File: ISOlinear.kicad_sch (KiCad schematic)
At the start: 23 parts, among them J1 USB_C_Receptacle_USB2.0, J2 Conn_01x20, J3 Conn_01x20, U1 STM32F072CBT6, U2 PRTR5V0U2X

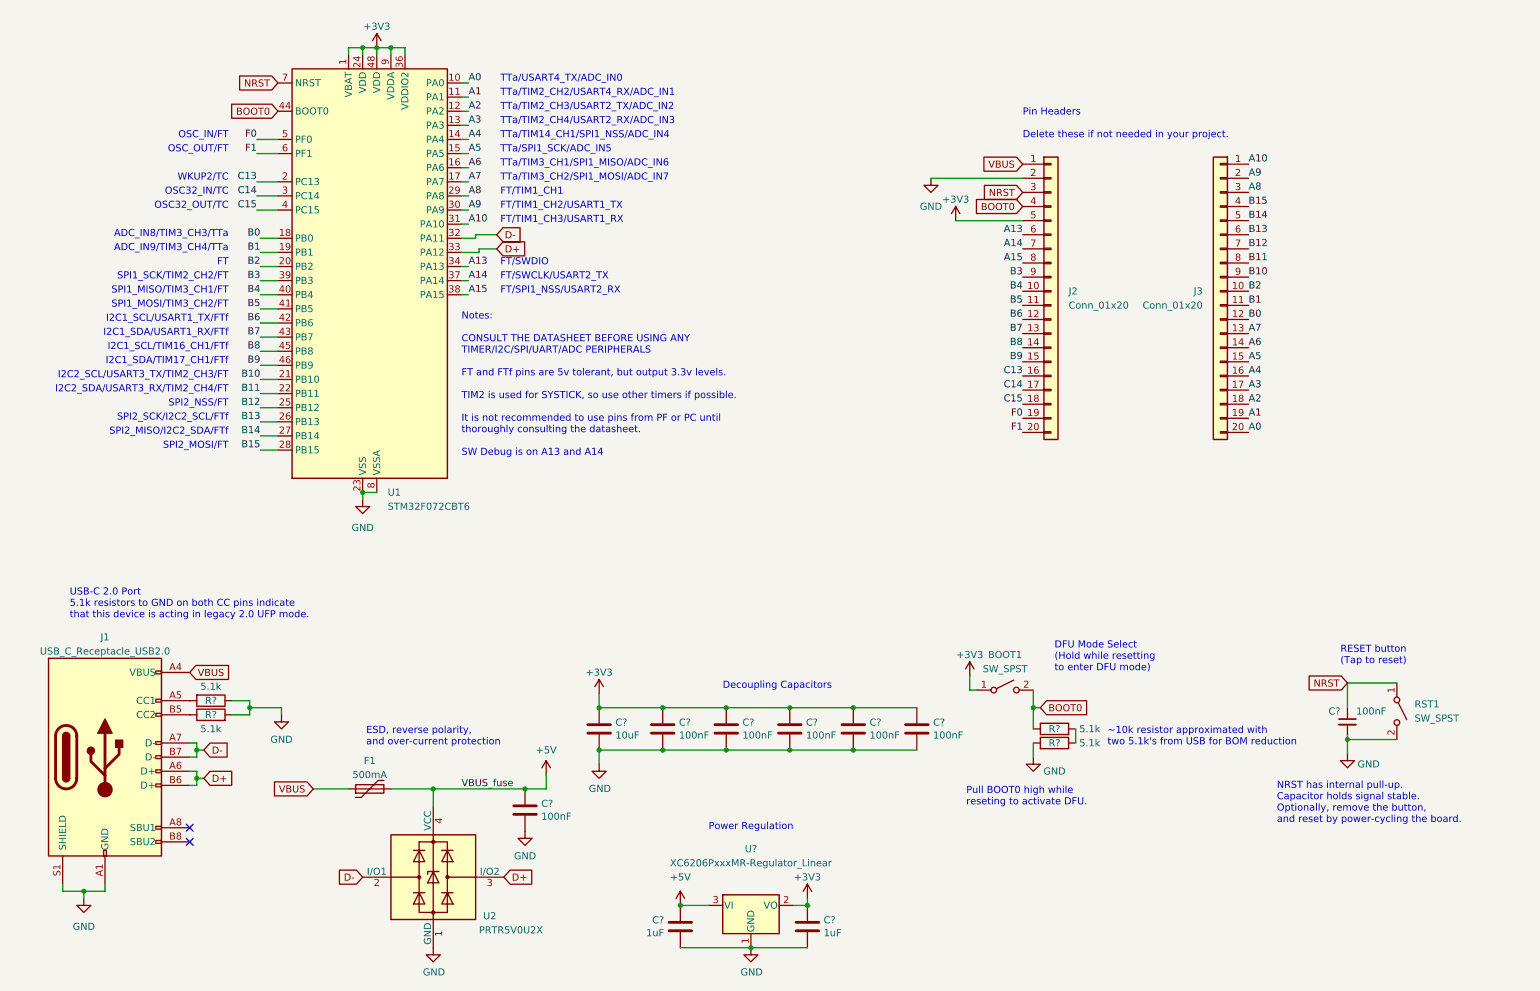
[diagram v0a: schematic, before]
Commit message: 1/21
Initial schematic/pcb setup, no routing and no global labels connected
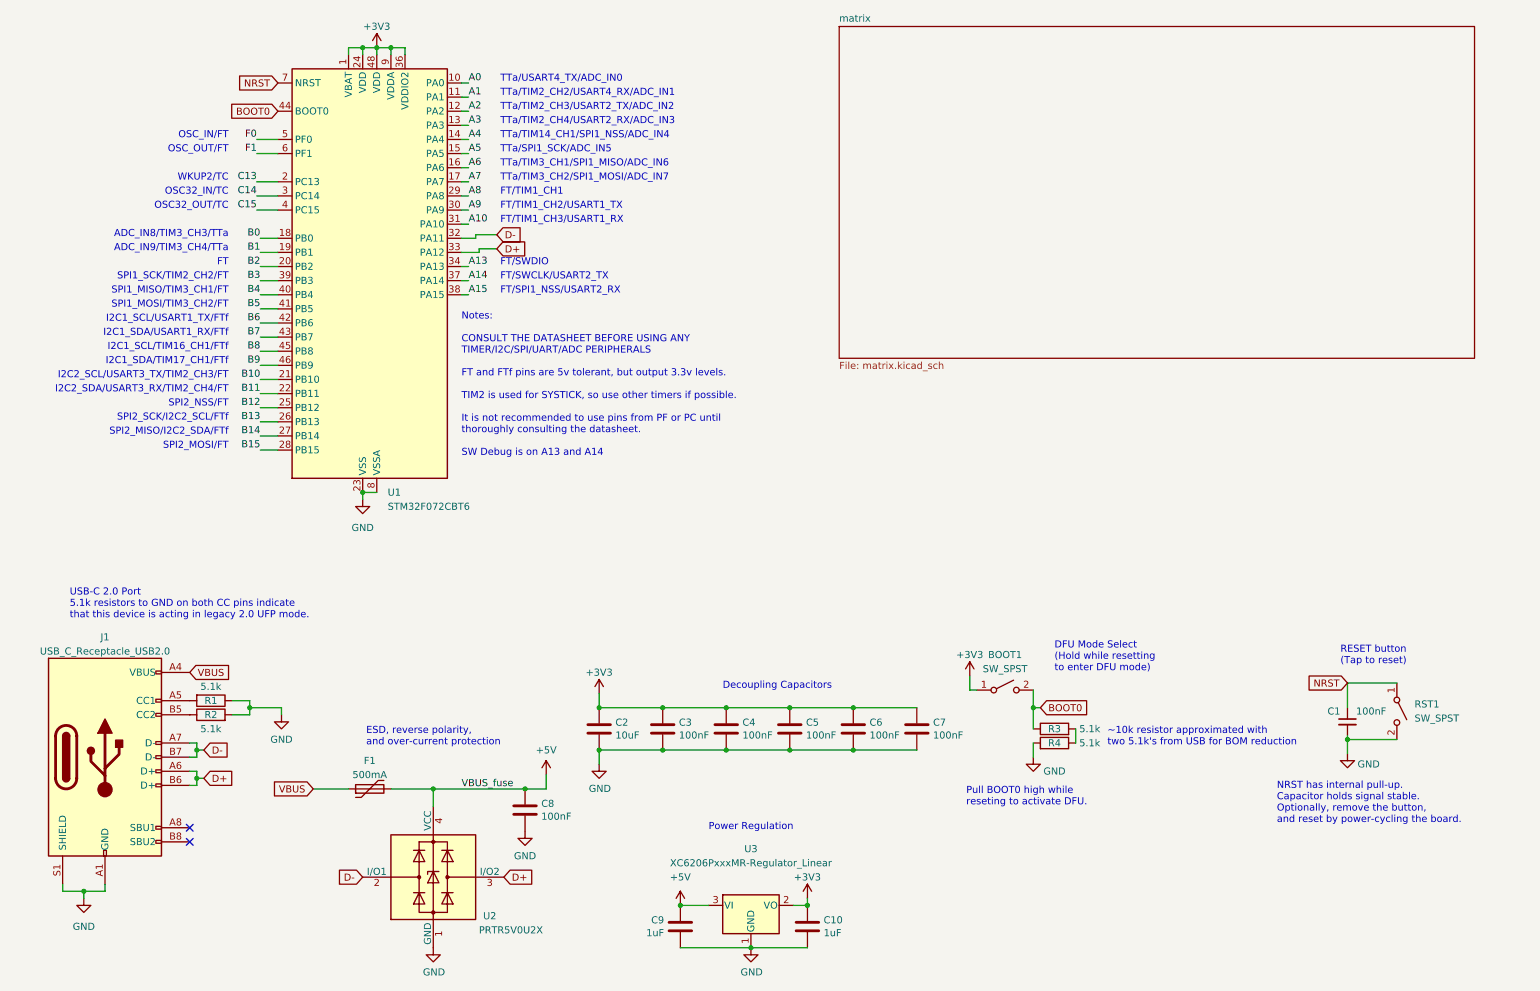
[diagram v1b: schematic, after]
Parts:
- removed J2, J3: Conn_01x20, Connector_PinHeader_2.54mm:PinHeader_1x20_P2.54mm_Vertical, symbol Connector_Generic:Conn_01x20
- gave numbers to parts that had none: 15
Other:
- added sheet matrix (matrix.kicad_sch)
- note removed: "Pin Headers Delete these if not needed in your project."

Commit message: 1/22
Routing solutions brainstorm
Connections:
- net A15 renamed ROW0
- net B3 renamed COL0
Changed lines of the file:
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@@
+	(wire
+		(pts
+			(xy 167.64 86.36) (xy 171.45 86.36)
+		)
+		(stroke
+			(width 0)
+			(type default)
+		)
+	)
 	(wire
 		(pts
@@
 	(wire
 		(pts
+			(xy 190.5 86.36) (xy 195.58 86.36)
+		)
+		(stroke
+			(width 0)
+			(type default)
+		)
+	)
+	(wire
+		(pts
 			(xy 60.96 68.58) (xy 64.135 68.58)
 		)
@@
 		(pts
 			(xy 33.02 175.895) (xy 33.02 174.625)
+		)
+		(stroke
+			(width 0)
+			(type default)
+		)
+	)
+	(wire
+		(pts
+			(xy 167.64 90.17) (xy 171.45 90.17)
 		)
 		(stroke
@@
 		)
 	)
+	(label "B3"
+		(at 190.5 86.36 180)
+		(effects
+			(font
+				(size 1.27 1.27)
+			)
+			(justify right bottom)
+		)
+	)
+	(label "A15"
+		(at 167.64 86.36 180)
+		(effects
+			(font
+				(size 1.27 1.27)
+			)
+			(justify right bottom)
+		)
+	)
 	(label "B14"
 		(at 60.96 93.98 180)
@@
 		)
 	)
+	(global_label "COL3"
+		(shape input)
+		(at 195.58 97.79 0)
+		(fields_autoplaced yes)
+		(effects
+			(font
+				(size 1.27 1.27)
+			)
+			(justify left)
+		)
+		(property "Intersheetrefs" "${INTERSHEET_REFS}"
+			(at 203.4033 97.79 0)
+			(effects
+				(font
+					(size 1.27 1.27)
+				)
+				(justify left)
+				(hide yes)
+			)
+		)
+	)
+	(global_label "COL1"
+		(shape input)
+		(at 195.58 90.17 0)
+		(fields_autoplaced yes)
+		(effects
+			(font
+				(size 1.27 1.27)
+			)
+			(justify left)
+		)
+		(property "Intersheetrefs" "${INTERSHEET_REFS}"
+			(at 203.4033 90.17 0)
+			(effects
+				(font
+					(size 1.27 1.27)
+				)
+				(justify left)
+				(hide yes)
+			)
+		)
+	)
 	(global_label "VBUS"
 		(shape input)
@@
 		)
 	)
+	(global_label "ROW2"
+		(shape input)
+		(at 171.45 93.98 0)
+		(fields_autoplaced yes)
+		(effects
+			(font
+				(size 1.27 1.27)
+			)
+			(justify left)
+		)
+		(property "Intersheetrefs" "${INTERSHEET_REFS}"
+			(at 179.6966 93.98 0)
+			(effects
+				(font
+					(size 1.27 1.27)
+				)
+				(justify left)
+				(hide yes)
+			)
+		)
+	)
 	(global_label "D-"
 		(shape input)
@@
 		)
 	)
+	(global_label "COL0"
+		(shape input)
+		(at 195.58 86.36 0)
+		(fields_autoplaced yes)
+		(effects
+			(font
+				(size 1.27 1.27)
+			)
+			(justify left)
+		)
+		(property "Intersheetrefs" "${INTERSHEET_REFS}"
+			(at 203.4033 86.36 0)
+			(effects
+				(font
+					(size 1.27 1.27)
+				)
+				(justify left)
+				(hide yes)
+			)
+		)
+	)
 	(global_label "BOOT0"
 		(shape input)
@@
 			(effects
 				(font
+					(size 1.27 1.27)
+				)
+				(justify left)
+				(hide yes)
+			)
+		)
+	)
+	(global_label "COL2"
+		(shape input)
+		(at 195.58 93.98 0)
+		(fields_autoplaced yes)
+		(effects
+			(font
+				(size 1.27 1.27)
+			)
+			(justify left)
+		)
+		(property "Intersheetrefs" "${INTERSHEET_REFS}"
+			(at 203.4033 93.98 0)
+			(effects
+				(font
+					(size 1.27 1.27)
+				)
+				(justify left)
+				(hide yes)
+			)
+		)
+	)
+	(global_label "ROW0"
+		(shape input)
+		(at 171.45 86.36 0)
+		(fields_autoplaced yes)
+		(effects
+			(font
+				(size 1.27 1.27)
+			)
+			(justify left)
+		)
+		(property "Intersheetrefs" "${INTERSHEET_REFS}"
+			(at 179.6966 86.36 0)
+			(effects
+				(font
+					(size 1.27 1.27)
+				)
+				(justify left)
+				(hide yes)
+			)
+		)
+	)
+	(global_label "ROW3"
+		(shape input)
+		(at 171.45 97.79 0)
+		(fields_autoplaced yes)
+		(effects
+			(font
+				(size 1.27 1.27)
+			)
+			(justify left)
+		)
+		(property "Intersheetrefs" "${INTERSHEET_REFS}"
+			(at 179.6966 97.79 0)
+			(effects
+				(font
+					(size 1.27 1.27)
+				)
+				(justify left)
+				(hide yes)
+			)
+		)
+	)
+	(global_label "ROW1"
+		(shape input)
+		(at 171.45 90.17 0)
+		(fields_autoplaced yes)
+		(effects
+			(font
+				(size 1.27 1.27)
+			)
+			(justify left)
+		)
+		(property "Intersheetrefs" "${INTERSHEET_REFS}"
+			(at 179.6966 90.17 0)
+			(effects
+				(font

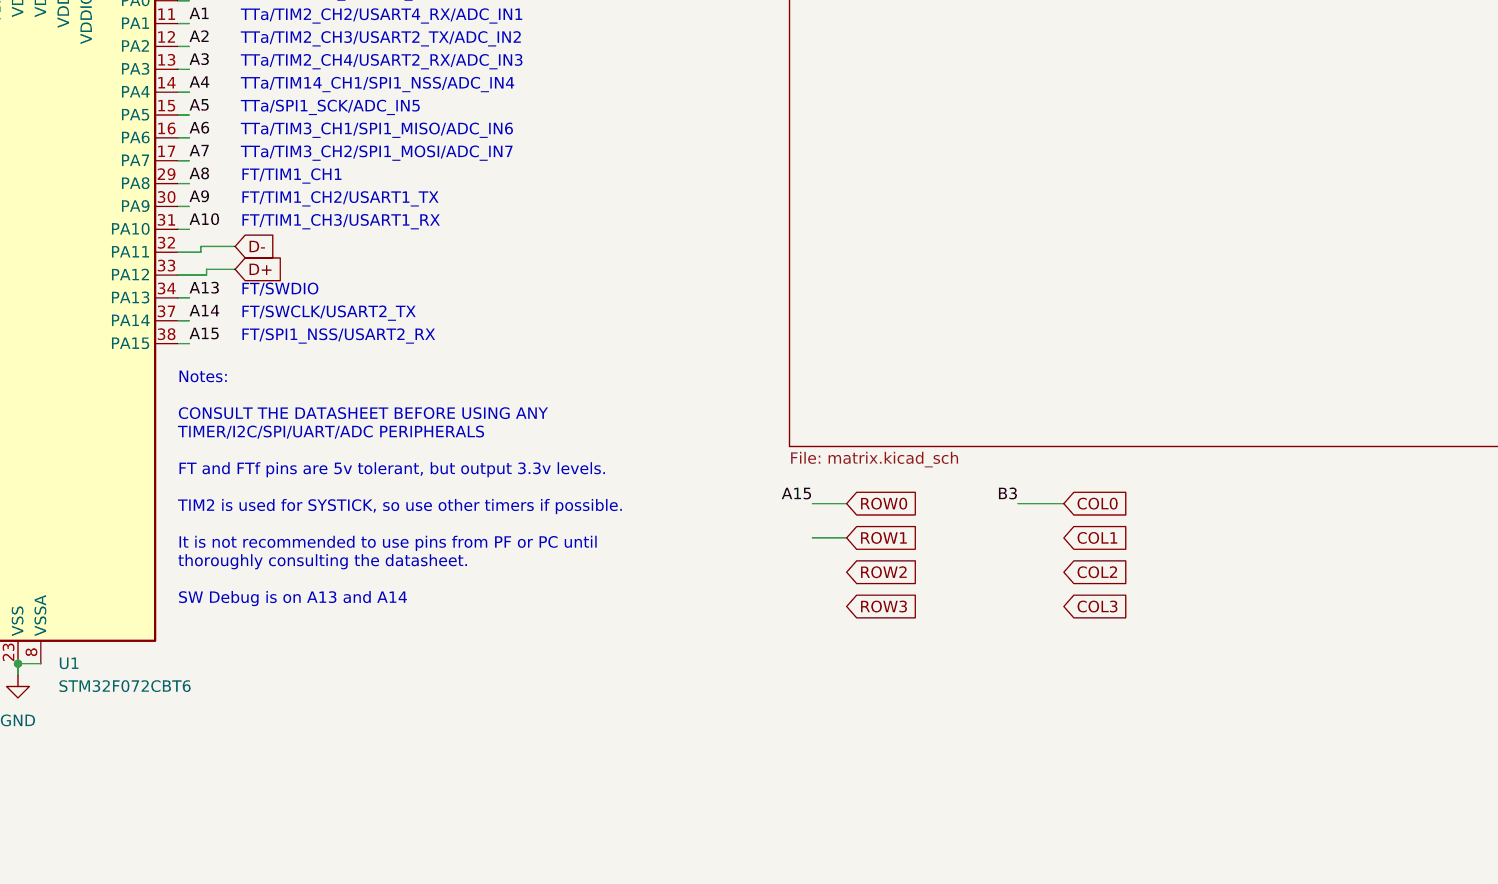
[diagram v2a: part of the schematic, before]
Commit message: 1/23
routed and filled tentatively, no grounds on some pins
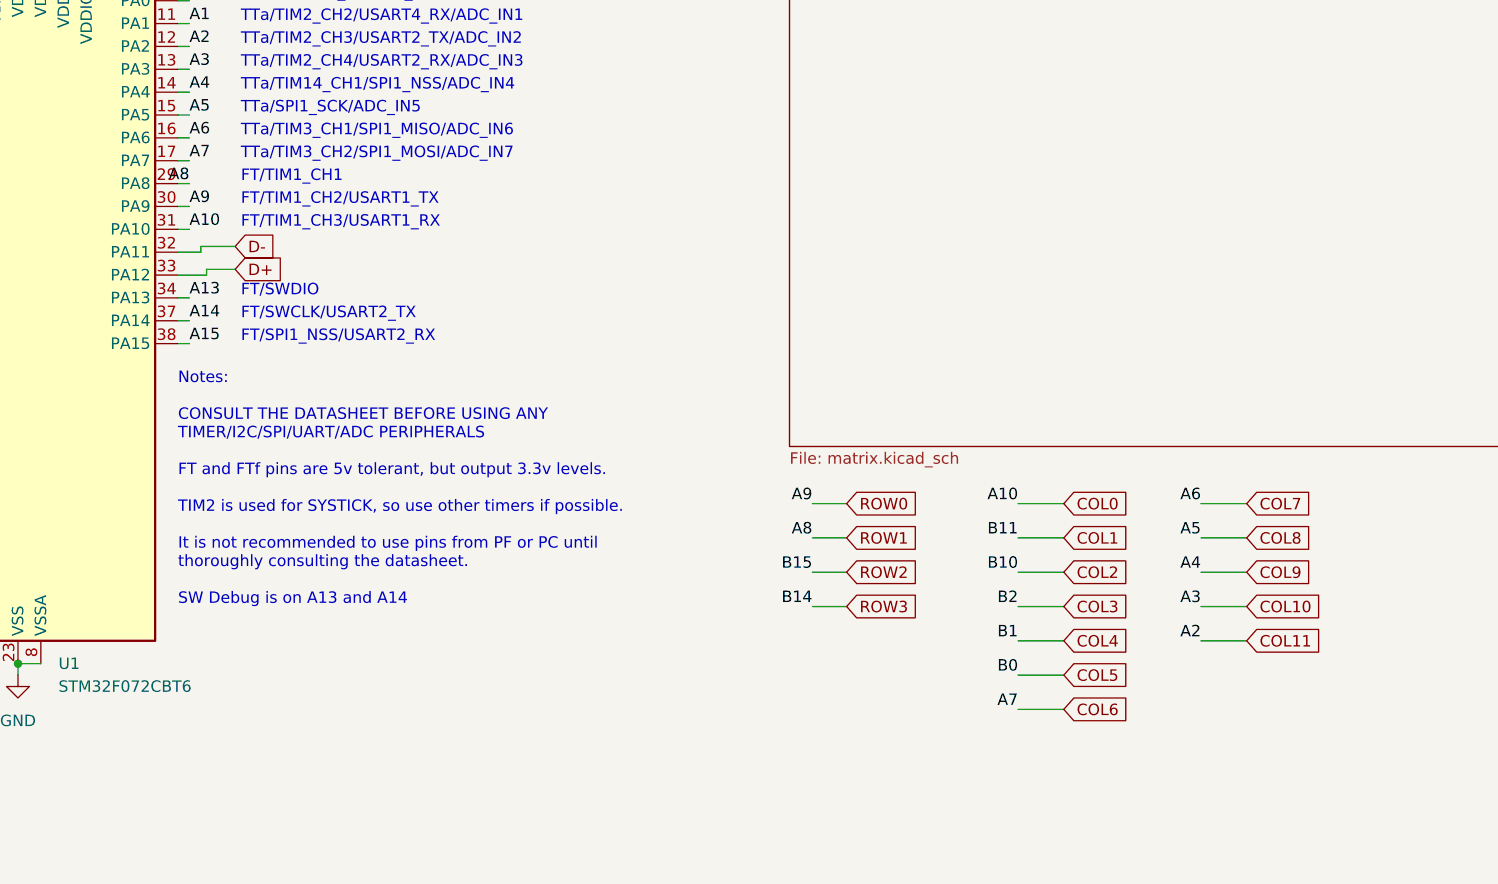
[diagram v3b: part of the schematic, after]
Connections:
- net A10 is gone; now on net COL0: U1.31 (PA10)
- net A8 is gone; now on net ROW1: U1.29 (PA8)
- net A9 is gone; now on net ROW0: U1.30 (PA9)
- net B10 is gone; now on net COL2: U1.21 (PB10)
- net B11 is gone; now on net COL1: U1.22 (PB11)
- net B14 is gone; now on net ROW3: U1.27 (PB14)
- net B15 is gone; now on net ROW2: U1.28 (PB15)
- net B2 is gone; now on net COL3: U1.20 (PB2)
- net COL0: no longer U1.39 (PB3)
- net ROW0: no longer U1.38 (PA15)
- net A2 renamed COL11
- net A3 renamed COL10
- net A4 renamed COL9
- net A5 renamed COL8
- net A6 renamed COL7
- net A7 renamed COL6
- net B0 renamed COL5
- net B1 renamed COL4
- new net A15: U1.38 (PA15)
- new net B3: U1.39 (PB3)
